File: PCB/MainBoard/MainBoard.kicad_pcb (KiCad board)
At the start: 2 copper layers, 100.1 x 78.2 mm, 30 parts, among them J1 Switch, J2 Prog Connector, J3 UART, J4 IR Connector, J5 Conn_01x02_Pin, J6 Conn_01x02_Pin, SW1 RESET_SW, U1 MCP1700-3302E/TO, U2 ATmega4808-A

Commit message: More main
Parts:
- added C7: 10u, Capacitor_SMD:C_1206_3216Metric, F.Cu at (106.7, 71.1)
- added C8: 10u, Capacitor_SMD:C_1206_3216Metric, F.Cu at (83.8, 94.5)
- added D5: SB130, Diode_THT:D_DO-41_SOD81_P7.62mm_Horizontal, F.Cu at (96.5, 61.0)
- added D6: SB130, Diode_THT:D_DO-41_SOD81_P7.62mm_Horizontal, F.Cu at (91.2, 110.5)
- added J7: Conn_01x02_Pin, Connector_PinHeader_2.54mm:PinHeader_1x02_P2.54mm_Vertical, F.Cu at (114.3, 61.0)
- added J8: Conn_01x02_Pin, Connector_PinHeader_2.54mm:PinHeader_1x02_P2.54mm_Vertical, F.Cu at (84.6, 99.6)
- added Q1: BSR802, Package_TO_SOT_SMD:SOT-23, F.Cu at (115.2, 69.5)
- added Q2: BSR802, Package_TO_SOT_SMD:SOT-23, F.Cu at (88.5, 93.8)
- added R10: 10000, Resistor_SMD:R_0805_2012Metric, F.Cu at (94.6, 93.0)
- added R11: 100, Resistor_SMD:R_0805_2012Metric, F.Cu at (94.8, 96.3)
- added R8: 10000, Resistor_SMD:R_0805_2012Metric, F.Cu at (99.1, 66.0)
- added R9: 100, Resistor_SMD:R_0805_2012Metric, F.Cu at (94.0, 66.0)
- J4: moved to B.Cu
- moved J4 2.17 mm to (172.7, 86.4), turned to 180 degrees
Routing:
- net GND: track 0.00 -> 66.6 mm
- net +6V: track 0.00 -> 44.7 mm
- net /R_MOTOR_PWM: track 0.00 -> 32.1 mm
- added copper zone on B.Cu, net GND

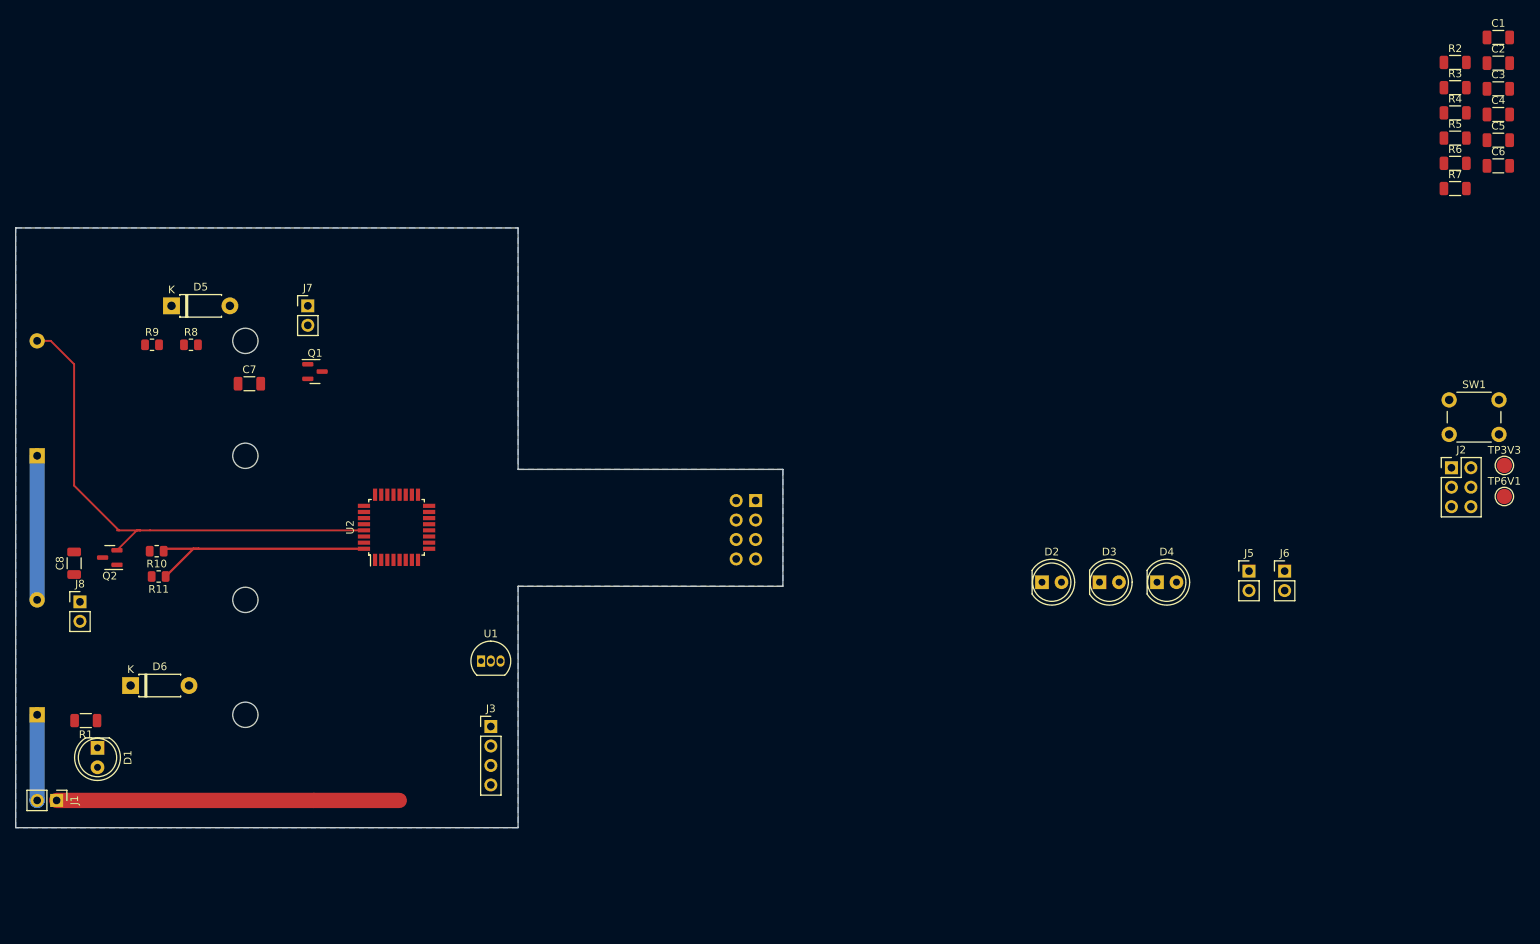
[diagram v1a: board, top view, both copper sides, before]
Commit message: Routed main board
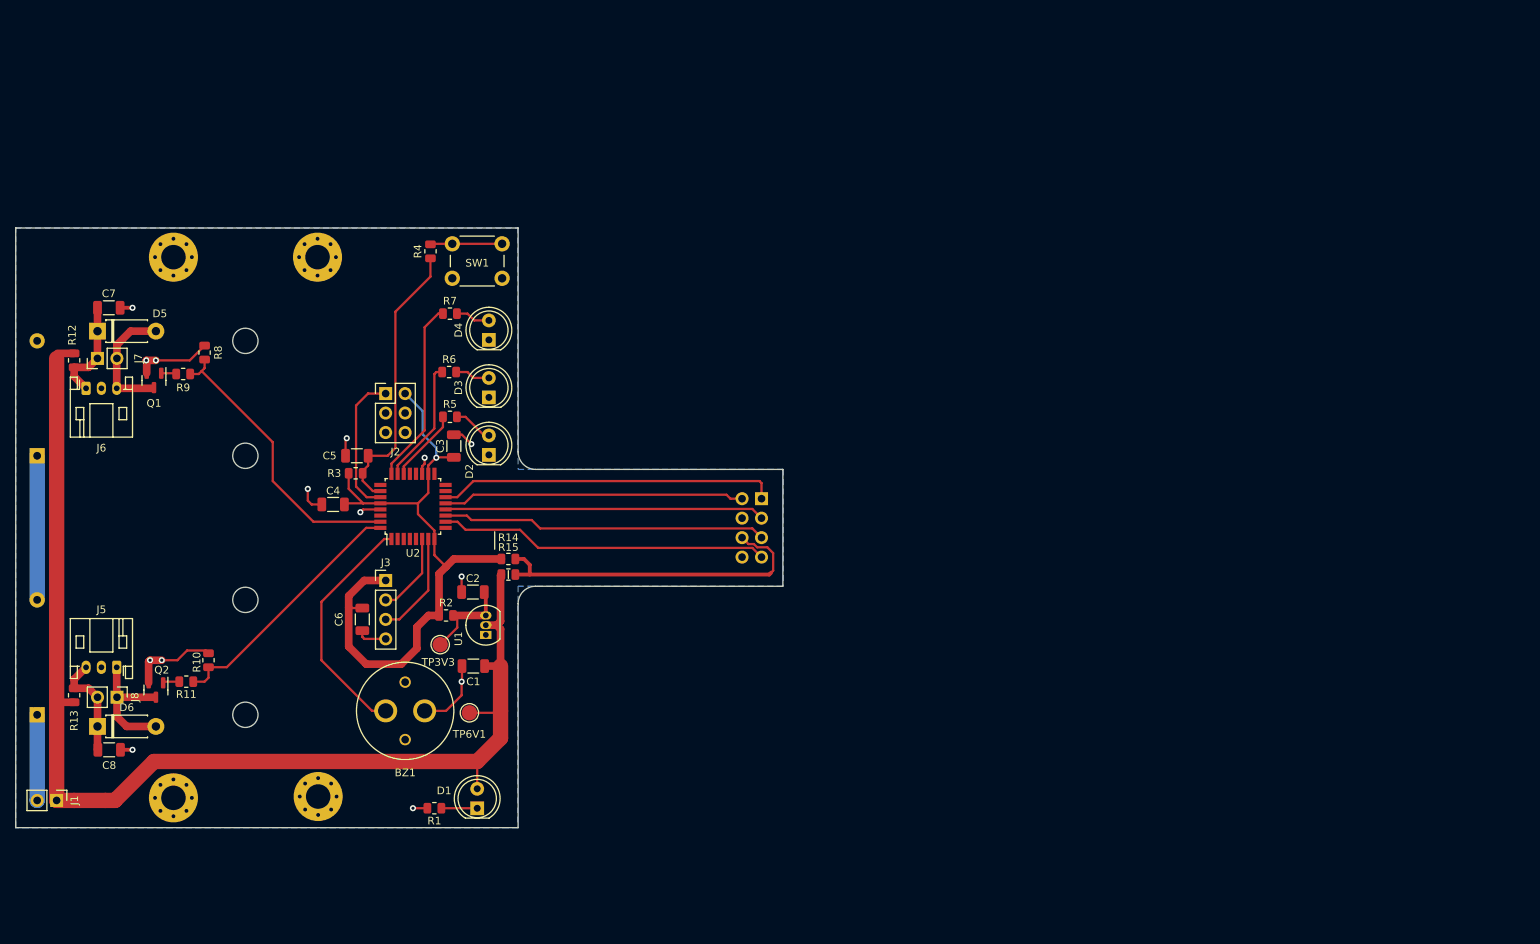
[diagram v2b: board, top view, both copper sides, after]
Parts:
- added BZ1: Buzzer, Custom:PKM13EPYH4000, F.Cu at (127.0, 113.8)
- added H1: MountingHole, MountingHole:MountingHole_3.2mm_M3_Pad_Via, F.Cu at (96.8, 54.6)
- added H2: MountingHole, MountingHole:MountingHole_3.2mm_M3_Pad_Via, F.Cu at (115.6, 54.6)
- added H3: MountingHole, MountingHole:MountingHole_3.2mm_M3_Pad_Via, F.Cu at (96.8, 125.1)
- added H4: MountingHole, MountingHole:MountingHole_3.2mm_M3_Pad_Via, F.Cu at (115.7, 125.0)
- added R12: 0R, Resistor_SMD:R_0805_2012Metric, F.Cu at (83.8, 68.1)
- added R13: 0R, Resistor_SMD:R_0805_2012Metric, F.Cu at (83.8, 111.8)
- added R14: 0R, Resistor_SMD:R_0805_2012Metric, F.Cu at (140.5, 94.0)
- added R15: 0R, Resistor_SMD:R_0805_2012Metric, F.Cu at (140.5, 96.0)
- J5: value Conn_01x02_Pin -> R Motor; footprint Connector_PinHeader_2.54mm:PinHeader_1x02_P2.54mm_Vertical -> Connector_JST:JST_PH_S3B-PH-K_1x03_P2.00mm_Horizontal
- J6: value Conn_01x02_Pin -> L_Motor; footprint Connector_PinHeader_2.54mm:PinHeader_1x02_P2.54mm_Vertical -> Connector_JST:JST_PH_S3B-PH-K_1x03_P2.00mm_Horizontal
- J7: value Conn_01x02_Pin -> L_Motor_Backup
- J8: value Conn_01x02_Pin -> R_Motor_Backup
- R1, R2, R3, R4, R5, R6, R7: footprint Resistor_SMD:R_1206_3216Metric -> Resistor_SMD:R_0805_2012Metric
- moved C4 160.3 mm to (117.6, 86.9), turned to 180 degrees
- moved C6 159.6 mm to (121.4, 101.9), turned to -90 degrees
- moved J6 158.2 mm to (85.4, 71.7)
- moved C1 156.8 mm to (135.9, 108.0), turned to 180 degrees
- moved C5 154.5 mm to (120.7, 80.5), turned to 180 degrees
- moved R3 152.0 mm to (120.5, 82.8)
- moved C2 150.5 mm to (135.8, 98.3), turned to 180 degrees
- moved R2 150.1 mm to (132.3, 101.3)
- moved J5 148.2 mm to (89.4, 108.1), turned to 180 degrees
- moved C3 144.0 mm to (133.3, 79.2), turned to 90 degrees
- moved TP3V3 140.8 mm to (131.6, 105.2)
- moved J2 139.4 mm to (124.5, 72.4)
- moved TP6V1 137.9 mm to (135.4, 114.0)
- moved R5 136.1 mm to (132.8, 75.4)
- moved R4 134.9 mm to (130.3, 53.8), turned to 90 degrees
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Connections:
- C7 pad 1: +6V -> Net-(D5-K)
- C8 pad 1: +6V -> Net-(D6-K)
- D5 pad 1: +6V -> Net-(D5-K)
- D6 pad 1: +6V -> Net-(D6-K)
- J4 pad 1: VCC -> /IR_5
- J4 pad 2: unconnected-(J4-Pin_2-Pad2) -> /IR_4
- J4 pad 3: /IR_1 -> /IR_3
- J4 pad 4: /IR_4 -> GND
- J4 pad 6: /IR_5 -> Net-(J4-Pin_6)
- J4 pad 7: /IR_3 -> /IR_1
- J5 pad 1: /L_MotorOut -> Net-(D6-A)
- J5 pad 2: GND -> unconnected-(J5-Pin_2-Pad2)
- J6 pad 1: /R_MotorOut -> Net-(D5-K)
- J6 pad 2: GND -> unconnected-(J6-Pin_2-Pad2)
- J7 pad 1: Net-(D5-A) -> Net-(D5-K)
- J7 pad 2: +6V -> Net-(D5-A)
- J8 pad 2: +6V -> Net-(D6-K)
- U2 pad 1: unconnected-(U2-PA3-Pad1) -> /BUZZER
- U2 pad 22: unconnected-(U2-PF2-Pad22) -> /LED_1
- U2 pad 23: unconnected-(U2-PF3-Pad23) -> /LED_2
- U2 pad 24: unconnected-(U2-PF4-Pad24) -> /LED_3
- U2 pad 8: unconnected-(U2-PC2-Pad8) -> +3V3
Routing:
- net +6V: track 44.7 -> 157.5 mm
- net +3V3: track 0.00 -> 88.9 mm, vias 0 -> 1
- net Net-(J4-Pin_6): track 0.00 -> 44.5 mm
- net /IR_5: track 0.00 -> 44.2 mm
- net /IR_1: track 0.00 -> 43.1 mm
- net /IR_2: track 0.00 -> 42.4 mm
- net /IR_3: track 0.00 -> 41.7 mm
- net /IR_4: track 0.00 -> 39.4 mm
- net /L_MOTOR_PWM: track 0.00 -> 37.7 mm
- net /RESET: track 0.00 -> 37.0 mm
- net /BUZZER: track 0.00 -> 31.3 mm
- net /LED_3: track 0.00 -> 24.0 mm
- net /UPDI_DATA: track 0.00 -> 18.8 mm
- net Net-(D6-A): track 0.00 -> 16.9 mm
- net /LED_2: track 0.00 -> 16.1 mm
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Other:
- outline, holes or cut-outs redrawn
- board text added: "-"

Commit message: Edits to both boards
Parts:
- added C10: C, Capacitor_THT:CP_Radial_D5.0mm_P2.50mm, F.Cu at (84.0, 63.0)
- added C9: C, Capacitor_THT:CP_Radial_D5.0mm_P2.50mm, F.Cu at (84.9, 122.9)
- added J9: Backup connector bit, Connector_PinHeader_2.00mm:PinHeader_1x05_P2.00mm_Vertical, F.Cu at (136.9, 91.9)
- moved R8 2.90 mm to (98.0, 67.8), turned to 180 degrees
- moved R10 2.84 mm to (98.6, 107.7), turned to 180 degrees
- moved R11 0.10 mm to (98.6, 110.0)
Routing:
- net +6V: track 157.5 -> 165.1 mm
- net GND: track 55.7 -> 51.4 mm
- net /R_MOTOR_PWM: track 33.5 -> 35.8 mm
- net /L_MOTOR_PWM: track 37.7 -> 40.0 mm
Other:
- board text added: "GND"
- board text added: "POWER JUMPER"

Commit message: Cleaned up repo
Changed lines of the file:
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@@
     (property "ki_keywords" "LED diode")
     (attr through_hole)
-    (fp_text reference "D2" (at -2.147 -2.54 90) (layer "F.SilkS")
+    (fp_text reference "D2" (at -1.893 -2.794 90) (layer "F.SilkS")
         (effects (font (size 1 1) (thickness 0.15)))
     )

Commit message: Add files via upload
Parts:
- added ?: LOGO, LOGO, F.Cu at (156.0, 89.2)
- added ?: LOGO, LOGO, F.Cu at (92.8, 87.2)
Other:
- board text added: "Brad Kin Oliver Marcus"
- board text added: "THE ANKLE BREAKER"

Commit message: Version that was submitted
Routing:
- net GND: track 51.4 -> 49.9 mm
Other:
- board text added: "Group 28"
